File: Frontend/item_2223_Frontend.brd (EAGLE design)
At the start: 160 x 100 mm, 29 parts, among them K1 351, U3 SSD1306_128X64, X1 MSTBA2, X10 MSTBA2, X11 MSTBA2, X12 MSTBA2, X13 MSTBA2, X14 MSTBA2, X15 MSTBA2, X2 MSTBA2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

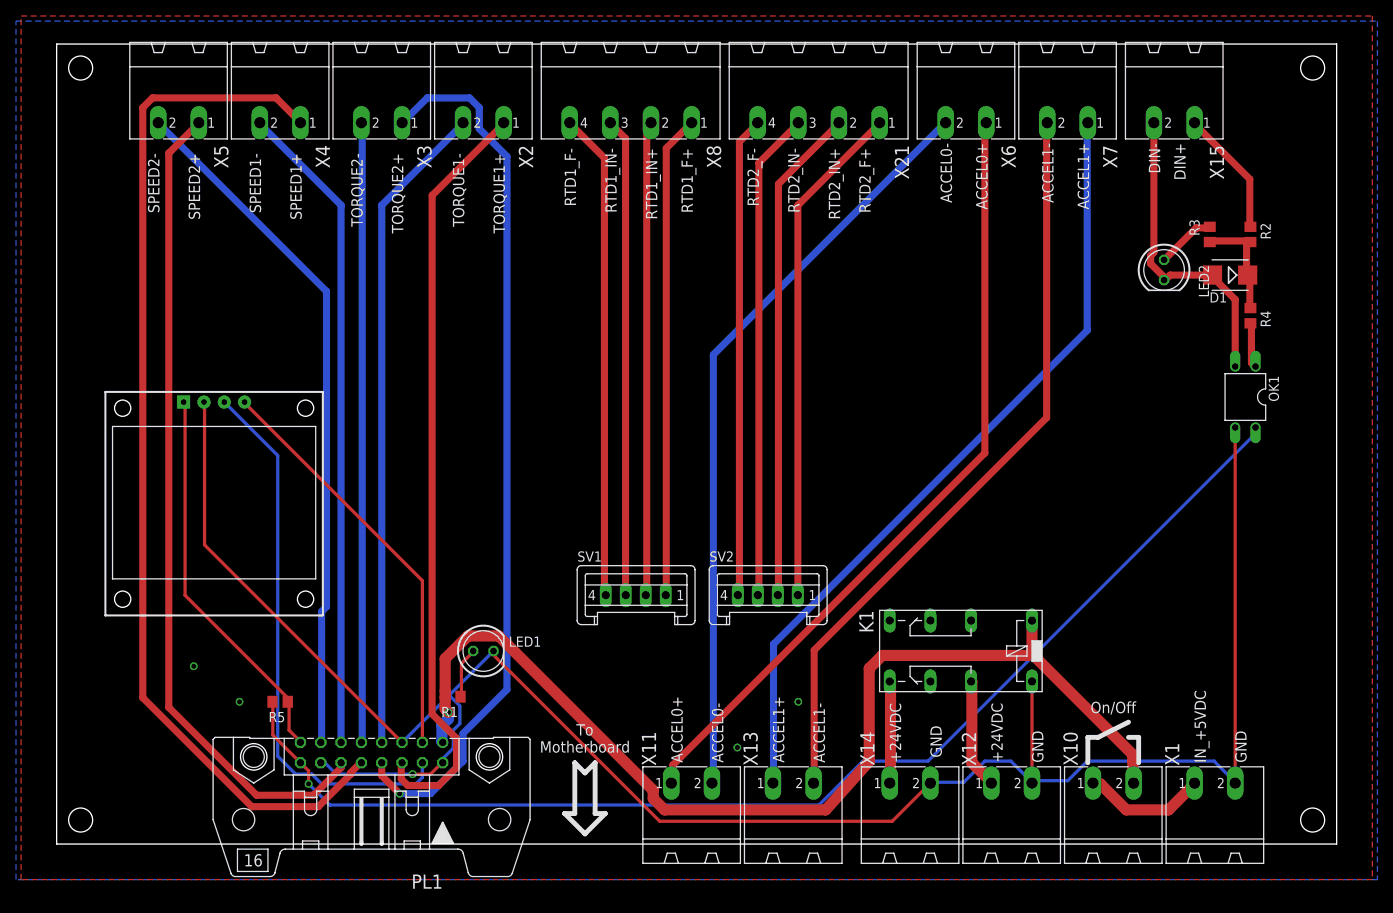
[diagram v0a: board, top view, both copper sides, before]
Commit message: Corretto GND di SSD1306 in Frontend e Motherboard
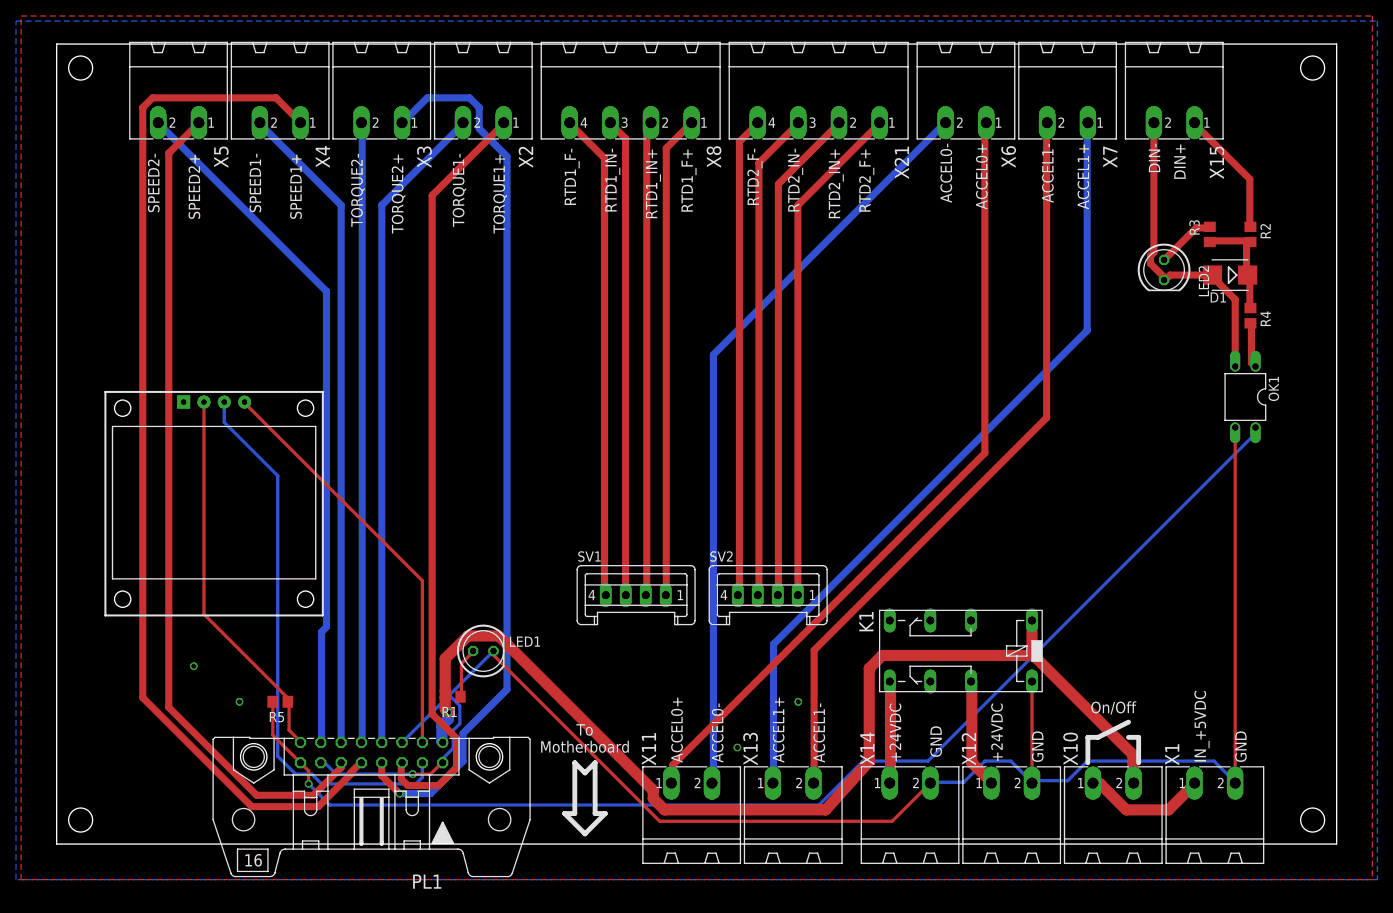
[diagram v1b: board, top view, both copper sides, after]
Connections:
- net +3V3: now also U3.2; no longer U3.VCC
- net GND: now also U3.1; no longer U3.GND
- net I2C_SCL: now also U3.3; no longer U3.SCL
- net I2C_SDA: now also U3.4; no longer U3.SDA
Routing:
- net GND: track 261.1 -> 208.3 mm
- net +3V3: track 48.6 -> 47.6 mm
